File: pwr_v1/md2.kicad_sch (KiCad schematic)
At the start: 17 parts, among them M2 Conn_01x08_Socket

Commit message: Schematic and layout updated
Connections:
- net GNDREF: no longer 2C6.2, 2U1.4 (GND_BK), M2.4 (Pin_4)
- new net GND_BK: 2C6.2, 2U1.4 (GND_BK), M2.4 (Pin_4)
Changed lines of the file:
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@@
-	)
-	(junction
-		(at 200.914 68.58)
-		(diameter 0)
-		(color 0 0 0 0)
 	)
 	(junction
@@
 	)
 	(junction
-		(at 122.174 49.149)
-		(diameter 0)
-		(color 0 0 0 0)
-	)
-	(junction
 		(at 136.144 110.49)
 		(diameter 0)
@@
 	)
 	(junction
-		(at 134.874 49.149)
-		(diameter 0)
-		(color 0 0 0 0)
-	)
-	(junction
 		(at 193.294 91.44)
 		(diameter 0)
@@
 	(wire
 		(pts
+			(xy 122.174 49.149) (xy 122.174 55.88)
+		)
+		(stroke
+			(width 0)
+			(type default)
+		)
+	)
+	(wire
+		(pts
 			(xy 155.194 54.61) (xy 155.194 55.88)
 		)
@@
 	(wire
 		(pts
-			(xy 200.914 49.149) (xy 200.914 68.58)
-		)
-		(stroke
-			(width 0)
-			(type default)
-		)
-	)
-	(wire
-		(pts
-			(xy 200.914 49.149) (xy 134.874 49.149)
-		)
-		(stroke
-			(width 0)
-			(type default)
-		)
-	)
-	(wire
-		(pts
 			(xy 181.864 102.87) (xy 209.804 102.87)
 		)
@@
 	(wire
 		(pts
-			(xy 116.84 49.149) (xy 122.174 49.149)
-		)
-		(stroke
-			(width 0)
-			(type default)
-		)
-	)
-	(wire
-		(pts
 			(xy 143.764 68.58) (xy 147.574 68.58)
 		)
@@
 	(wire
 		(pts
-			(xy 193.294 91.44) (xy 193.294 92.71)
-		)
-		(stroke
-			(width 0)
-			(type default)
-		)
-	)
-	(wire
-		(pts
 			(xy 221.234 120.65) (xy 246.634 120.65)
 		)
@@
 		(pts
 			(xy 190.754 63.5) (xy 211.074 63.5)
-		)
-		(stroke
-			(width 0)
-			(type default)
-		)
-	)
-	(wire
-		(pts
-			(xy 122.174 49.149) (xy 122.174 55.88)
 		)
 		(stroke
@@
 	(text "AVDD 3.3V/30mA"
 		(exclude_from_sim no)
-		(at 178.943 48.895 0)
+		(at 120.65 45.974 0)
 		(effects
 			(font
@@
 	)
 	(label "AVDD"
-		(at 116.84 49.149 0)
+		(at 122.174 49.276 0)
 		(fields_autoplaced yes)
 		(effects
@@
 					(unit 1)
 				)
-			)
-		)
-	)
-	(symbol
-		(lib_id "power:GNDREF")
-		(at 193.294 92.71 0)
-		(unit 1)
-		(exclude_from_sim no)
-		(in_bom yes)
-		(on_board yes)
-		(dnp no)
-		(property "Reference" "#PWR029"
-			(at 193.294 99.06 0)
-			(effects
-				(font
-					(size 1.27 1.27)
-				)
-				(hide yes)
-			)
-		)
-		(property "Value" "GNDREF"
-			(at 193.294 96.52 0)
-			(effects
-				(font
-					(size 1.27 1.27)
-				)
-				(hide yes)
-			)
-		)
-		(property "Footprint" ""
-			(at 193.294 92.71 0)
-			(effects
-				(font
-					(size 1.27 1.27)
-				)
-				(hide yes)
-			)
-		)
-		(property "Datasheet" ""
-			(at 193.294 92.71 0)
-			(effects
-				(font
-					(size 1.27 1.27)
-				)
-				(hide yes)
-			)
-		)
-		(property "Description" ""
-			(at 193.294 92.71 0)
-			(effects
-				(font
-					(size 1.27 1.27)
-				)
-				(hide yes)
-			)
-		)
-		(pin "1"
-		)
-		(instances
-			(project "pwr_v1"
-				(path "/42eee4f9-ea65-4e89-8296-df9554a24009/6744c016-77b4-4082-95f8-c8b724f132d7"
-					(reference "#PWR029")
-					(unit 1)
-				)

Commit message: Schematic updated
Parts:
- 2C1: footprint Capacitor_SMD:C_0805_2012Metric -> Capacitor_SMD:C_0402_1005Metric
- 2C2, 2C4, 2C6: footprint Capacitor_SMD:C_0603_1608Metric -> Capacitor_SMD:C_0402_1005Metric
- 2R1: footprint Resistor_SMD:R_0603_1608Metric_Pad0.98x0.95mm_HandSolder -> Resistor_SMD:R_0603_1608Metric

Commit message: Sch and Layout updated; Added batt sup ckt, placed and routed all motor drivers.
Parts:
- M2: footprint Connector_PinHeader_2.54mm:PinHeader_1x08_P2.54mm_Vertical_SMD_Pin1Left -> Connector_PinHeader_2.54mm:PinHeader_1x08_P2.54mm_Vertical
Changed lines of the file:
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@@
 			)
 		)
-		(property "Footprint" "Connector_PinHeader_2.54mm:PinHeader_1x08_P2.54mm_Vertical_SMD_Pin1Left"
+		(property "Footprint" "Connector_PinHeader_2.54mm:PinHeader_1x08_P2.54mm_Vertical"
 			(at 251.714 110.49 0)
 			(effects

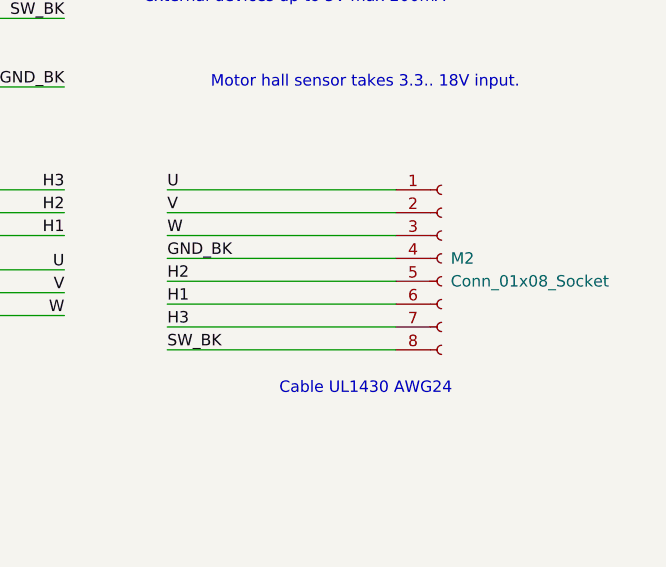
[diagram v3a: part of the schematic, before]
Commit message: Schematic and layout updated; Motor driver alignments and planes;  Few components updated
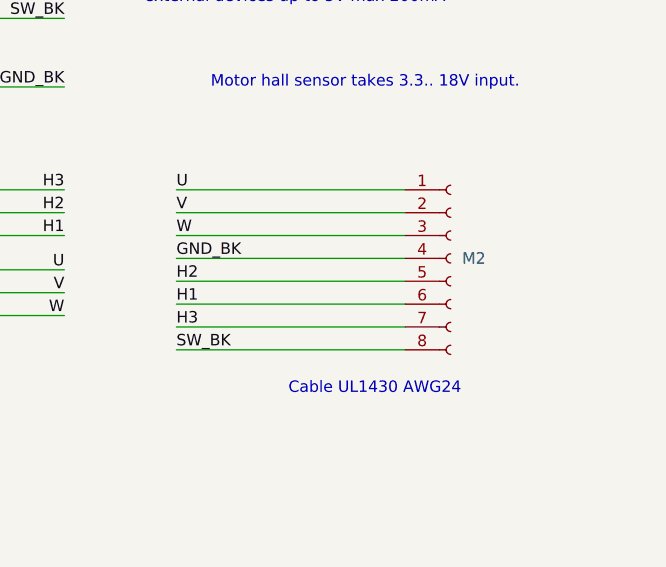
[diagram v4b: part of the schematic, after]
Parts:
- M2: footprint Connector_PinHeader_2.54mm:PinHeader_1x08_P2.54mm_Vertical -> Connector_Molex:Molex_KK-254_AE-6410-08A_1x08_P2.54mm_Vertical

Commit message: Schematic and layout updated; Layout placement and routing completed
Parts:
- M2: footprint Connector_Molex:Molex_KK-254_AE-6410-08A_1x08_P2.54mm_Vertical -> Connector_PinHeader_2.54mm:PinHeader_1x08_P2.54mm_Vertical
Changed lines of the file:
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@@
+	)
+	(symbol
+		(lib_id "Device:R_Small_US")
+		(at 128.524 58.42 0)
+		(unit 1)
+		(exclude_from_sim no)
+		(in_bom yes)
+		(on_board yes)
+		(dnp no)
+		(property "Reference" "2R2"
+			(at 129.794 57.658 0)
+			(effects
+				(font
+					(size 1.27 1.27)
+				)
+				(justify left)
+			)
+		)
+		(property "Value" "5k1"
+			(at 129.794 59.436 0)
+			(effects
+				(font
+					(size 1.27 1.27)
+				)
+				(justify left)
+			)
+		)
+		(property "Footprint" "Resistor_SMD:R_0603_1608Metric"
+			(at 128.524 58.42 0)
+			(effects
+				(font
+					(size 1.27 1.27)
+				)
+				(hide yes)
+			)
+		)
+		(property "Datasheet" "~"
+			(at 128.524 58.42 0)
+			(effects
+				(font
+					(size 1.27 1.27)
+				)
+				(hide yes)
+			)
+		)
+		(property "Description" "MFR.Part # ERJ3GEYJ512V JLCPCB Part # C403509"
+			(at 128.524 58.42 0)
+			(effects
+				(font
+					(size 1.27 1.27)
+				)
+				(hide yes)
+			)
+		)
+		(pin "1"
+		)
+		(pin "2"
+		)
+		(instances
+			(project "pwr_v1"
+				(path "/42eee4f9-ea65-4e89-8296-df9554a24009/6744c016-77b4-4082-95f8-c8b724f132d7"
+					(reference "2R2")
+					(unit 1)
+				)
+			)
+		)
+	)
+	(symbol
+		(lib_id "power:GNDREF")
+		(at 165.354 135.89 0)
+		(unit 1)
+		(exclude_from_sim no)
+		(in_bom yes)
+		(on_board yes)
+		(dnp no)
+		(property "Reference" "#PWR027"
+			(at 165.354 142.24 0)
+			(effects
+				(font
+					(size 1.27 1.27)
+				)
+				(hide yes)
+			)
+		)
+		(property "Value" "GNDREF"
+			(at 165.354 139.7 0)
+			(effects
+				(font
+					(size 1.27 1.27)
+				)
+				(hide yes)
+			)
+		)
+		(property "Footprint" ""
+			(at 165.354 135.89 0)
+			(effects
+				(font
+					(size 1.27 1.27)
+				)
+				(hide yes)
+			)
+		)
+		(property "Datasheet" ""
+			(at 165.354 135.89 0)
+			(effects
+				(font
+					(size 1.27 1.27)
+				)
+				(hide yes)
+			)
+		)
+		(property "Description" ""
+			(at 165.354 135.89 0)
+			(effects
+				(font
+					(size 1.27 1.27)
+				)
+				(hide yes)
+			)
+		)
+		(pin "1"
+		)
+		(instances
+			(project "pwr_v1"
+				(path "/42eee4f9-ea65-4e89-8296-df9554a24009/6744c016-77b4-4082-95f8-c8b724f132d7"
+					(reference "#PWR027")
+					(unit 1)
+				)
+			)
+		)
 	)
 	(symbol
@@
 			)
 		)
-		(property "Footprint" "Connector_Molex:Molex_KK-254_AE-6410-08A_1x08_P2.54mm_Vertical"
+		(property "Footprint" "Connector_PinHeader_2.54mm:PinHeader_1x08_P2.54mm_Vertical"
 			(at 252.73 110.49 0)
 			(effects
@@
 					(unit 1)
 				)
-			)
-		)
-	)
-	(symbol
-		(lib_id "Device:R_Small_US")
-		(at 128.524 58.42 0)
-		(unit 1)
-		(exclude_from_sim no)
-		(in_bom yes)
-		(on_board yes)
-		(dnp no)
-		(property "Reference" "2R2"
-			(at 129.794 57.658 0)
-			(effects
-				(font
-					(size 1.27 1.27)
-				)
-				(justify left)
-			)
-		)
-		(property "Value" "5k1"
-			(at 129.794 59.436 0)
-			(effects
-				(font
-					(size 1.27 1.27)
-				)
-				(justify left)
-			)
-		)
-		(property "Footprint" "Resistor_SMD:R_0603_1608Metric"
-			(at 128.524 58.42 0)
-			(effects
-				(font
-					(size 1.27 1.27)
-				)
-				(hide yes)
-			)
-		)
-		(property "Datasheet" "~"
-			(at 128.524 58.42 0)
-			(effects
-				(font
-					(size 1.27 1.27)
-				)
-				(hide yes)
-			)
-		)
-		(property "Description" "MFR.Part # ERJ3GEYJ512V JLCPCB Part # C403509"
-			(at 128.524 58.42 0)
-			(effects
-				(font
-					(size 1.27 1.27)
-				)
-				(hide yes)
-			)
-		)
-		(pin "1"
-		)
-		(pin "2"
-		)
-		(instances
-			(project "pwr_v1"
-				(path "/42eee4f9-ea65-4e89-8296-df9554a24009/6744c016-77b4-4082-95f8-c8b724f132d7"
-					(reference "2R2")
-					(unit 1)
-				)
-			)
-		)
-	)
-	(symbol
-		(lib_id "power:GNDREF")
-		(at 165.354 135.89 0)
-		(unit 1)
-		(exclude_from_sim no)
-		(in_bom yes)
-		(on_board yes)
-		(dnp no)
-		(property "Reference" "#PWR027"
-			(at 165.354 142.24 0)
-			(effects
-				(font
-					(size 1.27 1.27)
-				)
-				(hide yes)
-			)
-		)
-		(property "Value" "GNDREF"
-			(at 165.354 139.7 0)
-			(effects
-				(font
-					(size 1.27 1.27)
-				)
-				(hide yes)
-			)
-		)
-		(property "Footprint" ""
-			(at 165.354 135.89 0)
-			(effects
-				(font
-					(size 1.27 1.27)
-				)
-				(hide yes)
-			)
-		)
-		(property "Datasheet" ""
-			(at 165.354 135.89 0)
-			(effects
-				(font
-					(size 1.27 1.27)
-				)
-				(hide yes)
-			)
-		)
-		(property "Description" ""
-			(at 165.354 135.89 0)
-			(effects
-				(font
-					(size 1.27 1.27)
-				)
-				(hide yes)
-			)
-		)
-		(pin "1"
-		)
-		(instances
-			(project "pwr_v1"
-				(path "/42eee4f9-ea65-4e89-8296-df9554a24009/6744c016-77b4-4082-95f8-c8b724f132d7"
-					(reference "#PWR027")
-					(unit 1)
-				)

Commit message: Sch: 0ohm res added to SPI pins, MD footprints updated; Lay: Silkscreen aligned, logo added, DRC
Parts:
- 2U1: footprint MTR:RGF0040E-IPC_B -> motorDriver:RGF0040E-IPC_B
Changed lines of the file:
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@@
 			)
 		)
-		(property "Footprint" "MTR:RGF0040E-IPC_B"
+		(property "Footprint" "motorDriver:RGF0040E-IPC_B"
 			(at 223.774 60.96 0)
 			(effects

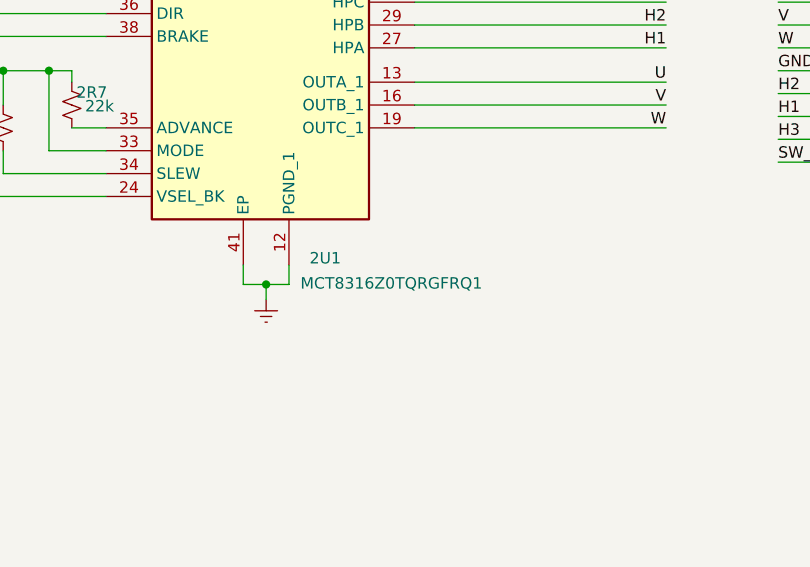
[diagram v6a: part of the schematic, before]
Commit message: Sch: DNP updated, JLC part numbers updated for all components; Lay: Fiducial placement, routing aligned.
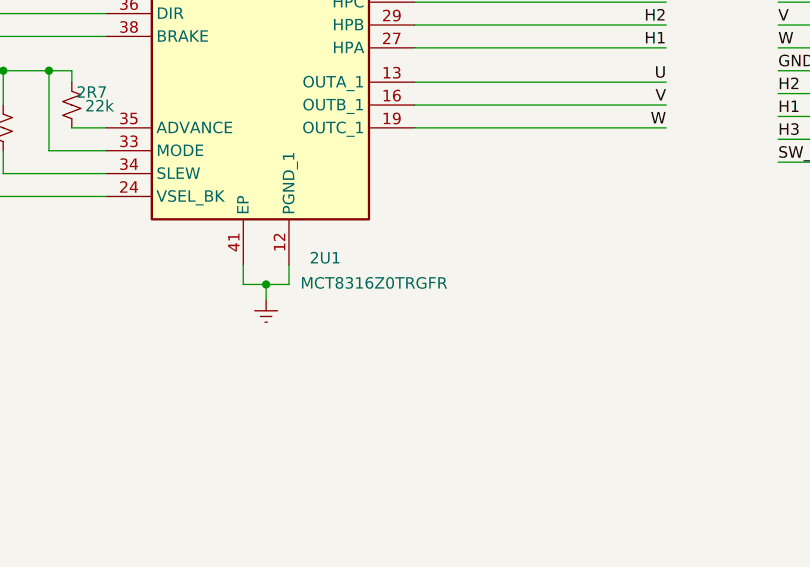
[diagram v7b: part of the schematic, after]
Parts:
- 2U1: value MCT8316Z0TQRGFRQ1 -> MCT8316Z0TRGFR
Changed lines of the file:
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@@
 			)
 		)
-		(property "Description" "Resistor, small US symbol"
+		(property "Description" "MFR.Part # 0603WAF2002T5E JLCPCB Part # C4184"
 			(at 134.874 72.39 0)
 			(effects
@@
 			)
 		)
-		(property "Description" "Resistor, small US symbol"
+		(property "Description" "MFR.Part # 0402WGF4702TCE JLCPCB Part # C25792"
 			(at 136.144 116.84 0)
 			(effects
@@
 			)
 		)
-		(property "Description" "Resistor, small US symbol"
+		(property "Description" "MFR.Part # RC0805FR-071ML JLCPCB Part # C107700"
 			(at 129.794 116.84 0)
 			(effects
@@
 			)
 		)
-		(property "Description" "Resistor, small US symbol"
+		(property "Description" "MFR.Part # 0603WAF2702T5E JLCPCB Part # C22967"
 			(at 134.874 58.42 0)
 			(effects
@@
 			)
 		)
-		(property "Value" "MCT8316Z0TQRGFRQ1"
+		(property "Value" "MCT8316Z0TRGFR"
 			(at 169.164 134.112 0)
 			(effects
@@
 			)
 		)
-		(property "Description" ""
+		(property "Description" "MFR.Part # MCT8316Z0TRGFR JLCPCB Part # C3681342"
 			(at 147.574 73.66 0)
 			(effects
@@
 			)
 		)
-		(property "Description" "Resistor, small US symbol"
+		(property "Description" "MFR.Part # 0402WGJ0223TCE JLCPCB Part # C25547"
 			(at 143.764 114.3 0)
 			(effects
@@
 			)
 		)
-		(property "Description" ""
+		(property "Description" "MFR.Part # HB-PH3-25418PB2GOP JLCPCB Part # C6332201"
 			(at 252.73 110.49 0)
 			(effects

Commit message: Final PCB files sent for fab
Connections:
- net GNDREF renamed GND
